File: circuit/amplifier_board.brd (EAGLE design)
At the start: 60 x 30 mm, 17 parts

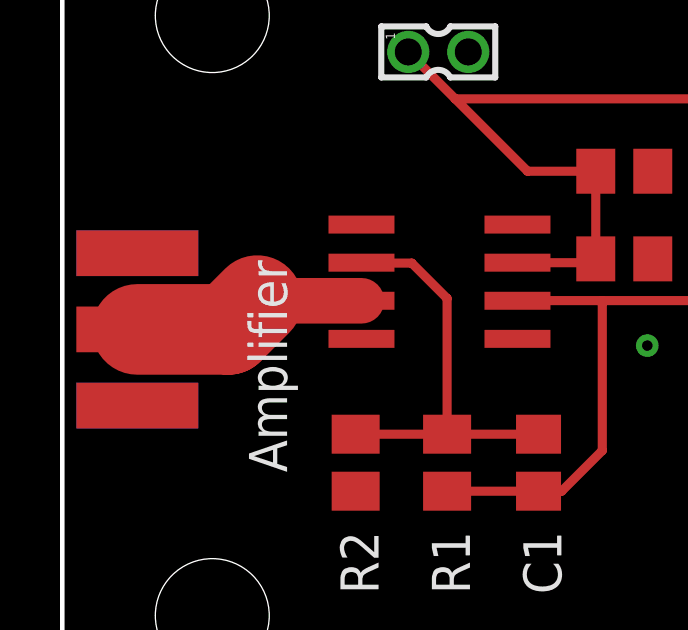
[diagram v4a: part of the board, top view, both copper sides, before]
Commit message: boards: Changes to amplifier board board.
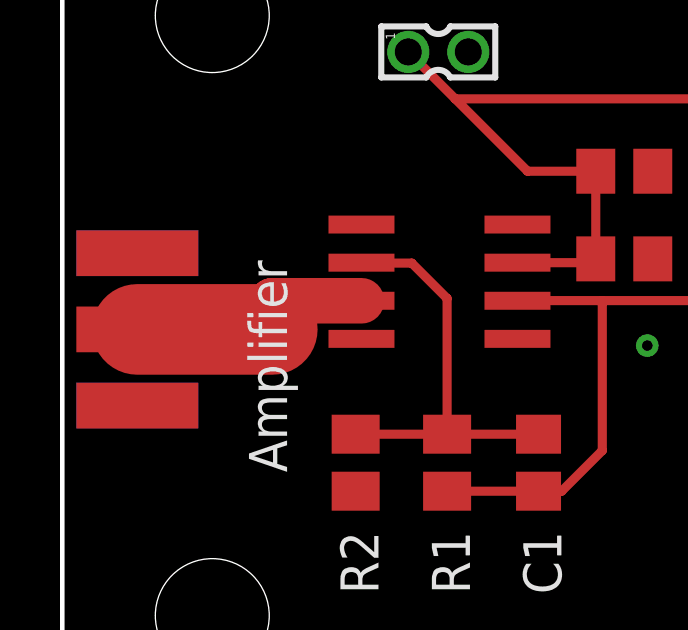
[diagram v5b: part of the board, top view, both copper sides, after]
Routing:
- net IN: track 7.87 -> 8.43 mm
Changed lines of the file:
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@@
 <drawing>
 <settings>
-<setting alwaysvectorfont="no"/>
+<setting alwaysvectorfont="yes"/>
 <setting verticaltext="up"/>
 </settings>
@@
 <contactref element="MAX4104_1" pad="3"/>
 <contactref element="IN" pad="SIG"/>
-<wire x1="2.5" y1="14.54" x2="5.54" y2="14.54" width="3.021" layer="1"/>
-<wire x1="6.5" y1="15.5" x2="5.54" y2="14.54" width="3.021" layer="1"/>
-<wire x1="9.973" y1="15.494" x2="6.506" y2="15.494" width="1.52" layer="1"/>
-<wire x1="6.506" y1="15.494" x2="6.5" y2="15.5" width="1.52" layer="1"/>
+<wire x1="2.5" y1="14.54" x2="7" y2="14.54" width="3.021" layer="1"/>
+<wire x1="9.973" y1="15.494" x2="7" y2="15.494" width="1.52" layer="1"/>
+<wire x1="7" y1="15.494" x2="7" y2="14.54" width="1.52" layer="1"/>
 </signal>
 </signals>

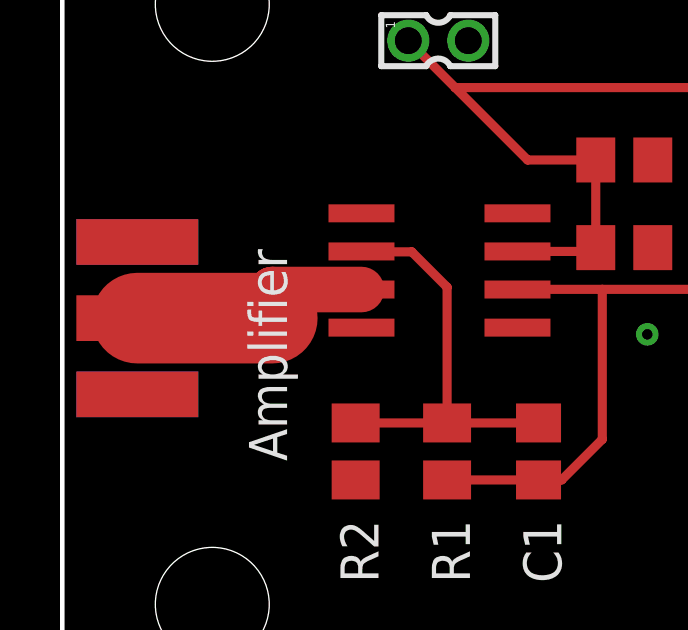
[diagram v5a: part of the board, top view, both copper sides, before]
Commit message: boards: Simplified both boards
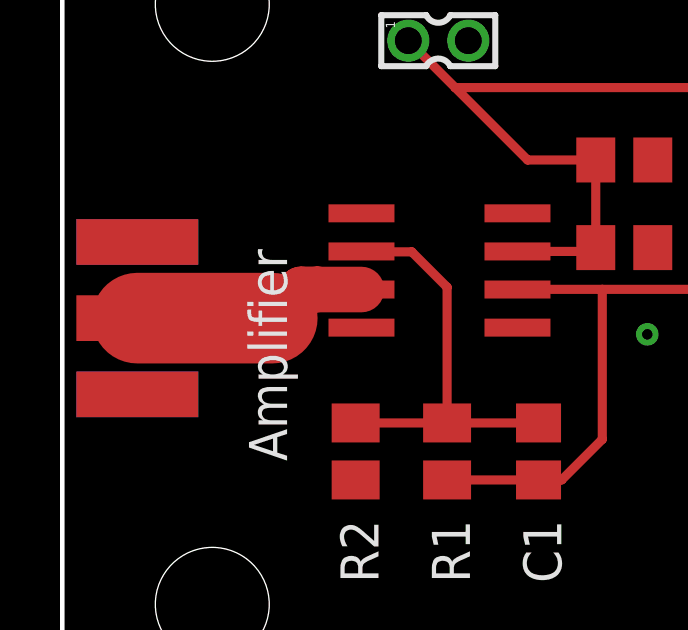
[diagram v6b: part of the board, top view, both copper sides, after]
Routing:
- net IN: track 8.43 -> 7.87 mm
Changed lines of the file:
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@@
 <drawing>
 <settings>
-<setting alwaysvectorfont="yes"/>
+<setting alwaysvectorfont="no"/>
 <setting verticaltext="up"/>
 </settings>
@@
 <contactref element="MAX4104_1" pad="3"/>
 <contactref element="IN" pad="SIG"/>
-<wire x1="2.5" y1="14.54" x2="7" y2="14.54" width="3.021" layer="1"/>
-<wire x1="9.973" y1="15.494" x2="7" y2="15.494" width="1.52" layer="1"/>
-<wire x1="7" y1="15.494" x2="7" y2="14.54" width="1.52" layer="1"/>
+<wire x1="7" y1="14.54" x2="2.5" y2="14.54" width="3.021" layer="1"/>
+<wire x1="9.973" y1="15.494" x2="8.506" y2="15.494" width="1.52" layer="1"/>
+<wire x1="8.506" y1="15.494" x2="8.5" y2="15.5" width="1.52" layer="1"/>
+<wire x1="8.5" y1="15.5" x2="7.96" y2="15.5" width="1.52" layer="1"/>
+<wire x1="7.96" y1="15.5" x2="7" y2="14.54" width="1.52" layer="1"/>
 </signal>
 </signals>

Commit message: boards: Rev00_ss ready
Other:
- board text added: "Gnd"
- board text added: "Out"
- board text added: "Rev00, amplifier board Asher Merrill & Maurik Holtrop, UNH 2018"
- board text added: "Vbias"
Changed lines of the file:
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@@
 <drawing>
 <settings>
-<setting alwaysvectorfont="no"/>
+<setting alwaysvectorfont="yes"/>
 <setting verticaltext="up"/>
 </settings>
@@
 <wire x1="60" y1="0" x2="60" y2="30" width="0.1524" layer="20"/>
 <wire x1="60" y1="30" x2="0" y2="30" width="0.1524" layer="20"/>
+<text x="12" y="22.5" size="1.778" layer="21" rot="R180">Vbias</text>
+<text x="13" y="25" size="1.778" layer="21">Gnd</text>
+<text x="54" y="15" size="1.778" layer="21" rot="R180">Out</text>
+<text x="54" y="17" size="1.778" layer="21" rot="R180">Gnd</text>
+<text x="9" y="2" size="1.2" layer="21">Rev00, amplifier board
+Asher Merrill &amp; Maurik Holtrop, UNH 2018</text>
 </plain>
 <attributes>
@@
 </drawing>
 <compatibility>
+<note version="6.3" minversion="6.2.2" severity="warning">
+Since Version 6.2.2 text objects can contain more than one line,
+which will not be processed correctly with this version.
+</note>
 <note version="8.2" severity="warning">
 Since Version 8.2, EAGLE supports online libraries. The ids

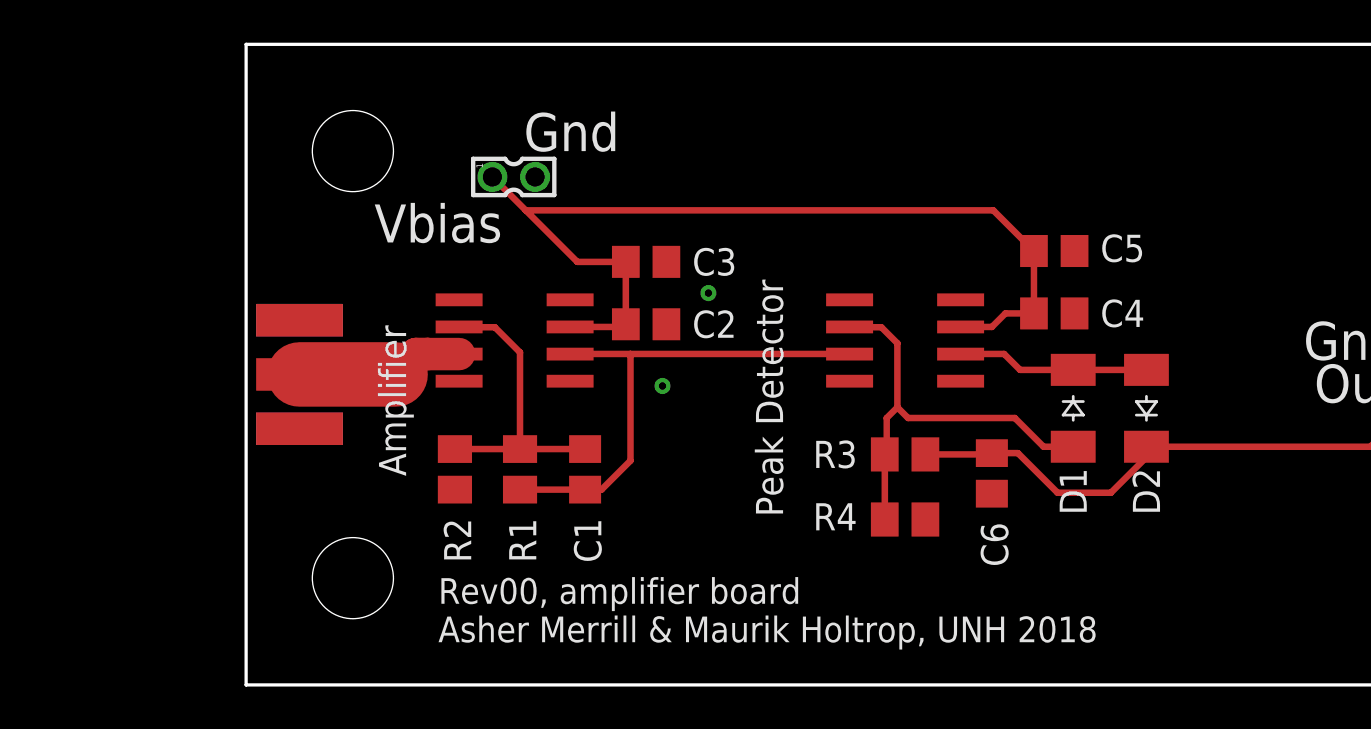
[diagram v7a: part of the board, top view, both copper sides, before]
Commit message: Modified board. Tried to add Spice model.
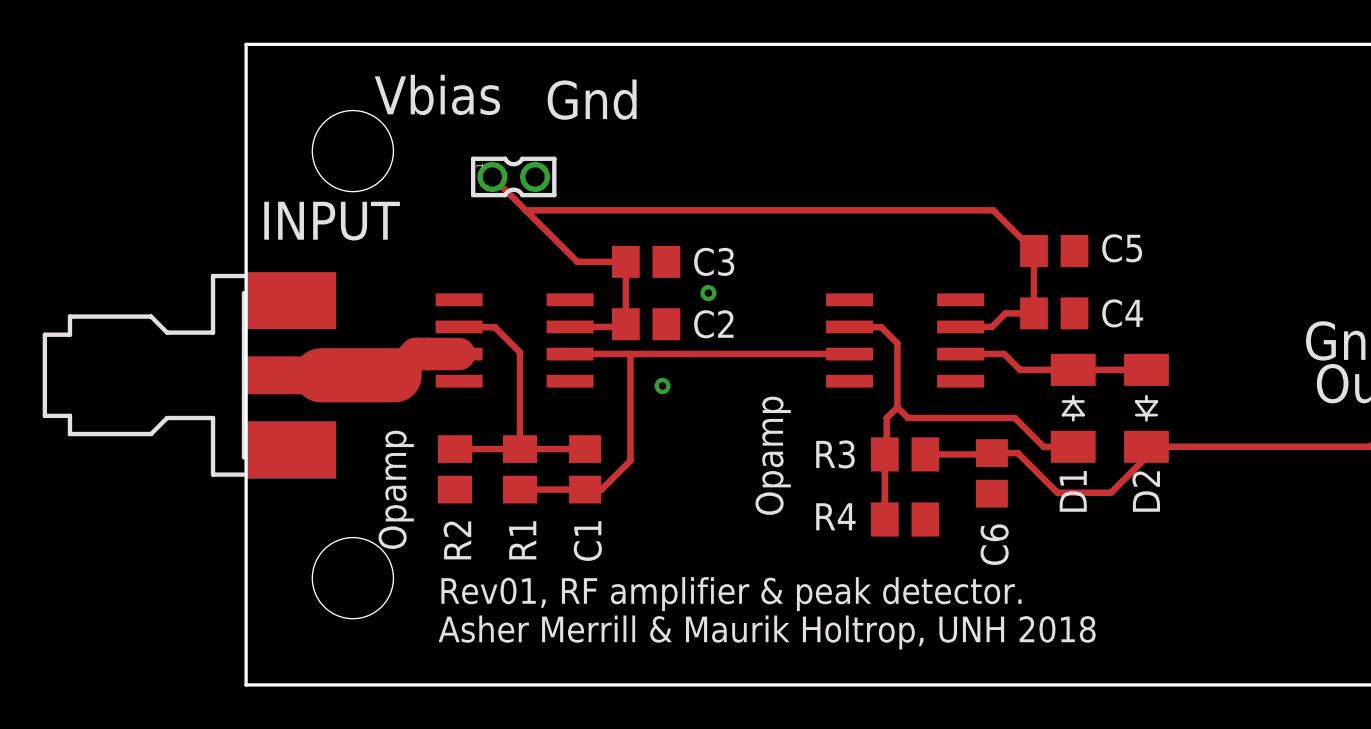
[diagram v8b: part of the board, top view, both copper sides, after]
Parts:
- removed IN: SMA_EDGE, SparkFun-Retired:SMA-EDGE
- added INPUT: SMA-EDGE, 000phys605parts:SMA-EDGE
- MAX4104_1: value Amplifier -> Opamp
- MAX4104_2: value Peak Detector -> Opamp
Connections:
- net GND: now also INPUT.G@1, INPUT.G@2, INPUT.G@3, INPUT.G@4; no longer IN.GND@0, IN.GND@1, IN.GND@2, IN.GND@3
- net IN: now also INPUT.G@0; no longer IN.SIG
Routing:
- net IN: track 7.87 -> 6.89 mm
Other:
- board text added: "Rev01, RF amplifier & peak detector. Asher Merrill & Maurik Holtrop, UNH 2018"
- board text removed: "Rev00, amplifier board Asher Merrill & Maurik Holtrop, UNH 2018"
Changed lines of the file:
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@@
 <drawing>
 <settings>
-<setting alwaysvectorfont="yes"/>
+<setting alwaysvectorfont="no"/>
 <setting verticaltext="up"/>
 </settings>
@@
 <wire x1="60" y1="0" x2="60" y2="30" width="0.1524" layer="20"/>
 <wire x1="60" y1="30" x2="0" y2="30" width="0.1524" layer="20"/>
-<text x="12" y="22.5" size="1.778" layer="21" rot="R180">Vbias</text>
-<text x="13" y="25" size="1.778" layer="21">Gnd</text>
+<text x="12" y="28.5" size="1.778" layer="21" rot="R180">Vbias</text>
+<text x="14" y="26.5" size="1.778" layer="21">Gnd</text>
 <text x="54" y="15" size="1.778" layer="21" rot="R180">Out</text>
 <text x="54" y="17" size="1.778" layer="21" rot="R180">Gnd</text>
-<text x="9" y="2" size="1.2" layer="21">Rev00, amplifier board
+<text x="9" y="2" size="1.2" layer="21">Rev01, RF amplifier &amp; peak detector.
 Asher Merrill &amp; Maurik Holtrop, UNH 2018</text>
 </plain>
@@
 <attribute name="SPICEPREFIX" value="C" x="15.875" y="10.0965" size="1.778" layer="27" rot="R90" display="off"/>
 </element>
-<element name="MAX4104_1" library="000phys605parts" package="SO8" value="Amplifier" x="12.573" y="16.129" smashed="yes" rot="R270">
-<attribute name="VALUE" x="7.493" y="9.779" size="1.27" layer="21" rot="R90"/>
+<element name="MAX4104_1" library="000phys605parts" package="SO8" value="Opamp" x="12.573" y="16.129" smashed="yes" rot="R270">
+<attribute name="SPICEMODEL" value="MAX4104" x="12.573" y="16.129" size="1.778" layer="27" rot="R270" display="off"/>
+<attribute name="SPICEPREFIX" value="X" x="12.573" y="16.129" size="1.778" layer="27" rot="R270" display="off"/>
+<attribute name="VALUE" x="7.493" y="6.279" size="1.27" layer="21" rot="R90"/>
 </element>
 <element name="R1" library="rcl" library_urn="urn:adsk.eagle:library:334" package="M0805" package3d_urn="urn:adsk.eagle:package:23556/1" value="10k" x="12.827" y="10.0965" smashed="yes" rot="R270">
@@
 <attribute name="SPICEPREFIX" value="C" x="18.7325" y="16.891" size="1.778" layer="27" display="off"/>
 </element>
-<element name="SUP" library="con-garry" library_urn="urn:adsk.eagle:library:147" package="332-02" package3d_urn="urn:adsk.eagle:package:6810/1" value="332-02" x="12.533" y="23.789" smashed="yes" rot="R270"/>
-<element name="MAX4104_2" library="000phys605parts" package="SO8" value="Peak Detector" x="30.861" y="16.129" smashed="yes" rot="R270">
+<element name="SUP" library="con-garry" library_urn="urn:adsk.eagle:library:147" package="332-02" package3d_urn="urn:adsk.eagle:package:6810/1" value="332-02" x="12.533" y="23.789" smashed="yes" rot="R270">
+<attribute name="SPICEMODEL" value="VoltageSource" x="12.533" y="23.789" size="1.778" layer="27" rot="R270" display="off"/>
+<attribute name="SPICEPREFIX" value="X" x="12.533" y="23.789" size="1.778" layer="27" rot="R270" display="off"/>
+</element>
+<element name="MAX4104_2" library="000phys605parts" package="SO8" value="Opamp" x="30.861" y="16.129" smashed="yes" rot="R270">
+<attribute name="SPICEMODEL" value="MAX4104" x="30.861" y="16.129" size="1.778" layer="27" rot="R270" display="off"/>
+<attribute name="SPICEPREFIX" value="X" x="30.861" y="16.129" size="1.778" layer="27" rot="R270" display="off"/>
 <attribute name="VALUE" x="25.146" y="7.874" size="1.27" layer="21" rot="R90"/>
 </element>
@@
 <attribute name="SPICEPREFIX" value="C" x="34.925" y="9.906" size="1.778" layer="27" rot="R270" display="off"/>
 </element>
-<element name="IN" library="SparkFun-Retired" package="SMA-EDGE" value="SMA_EDGE" x="2.5" y="12" rot="R90"/>
 <element name="D1" library="diode" library_urn="urn:adsk.eagle:library:210" package="SOD-123_MINI-SMA" package3d_urn="urn:adsk.eagle:package:43457/2" value="MBR0540CT-ND" x="38.735" y="12.954" smashed="yes" rot="R270">
 <attribute name="NAME" x="38.1" y="10.16" size="1.27" layer="25" rot="R270"/>
+<attribute name="SPICEMODEL" value="DMBR0540" x="38.735" y="12.954" size="1.778" layer="27" rot="R270" display="off"/>
+<attribute name="SPICEPREFIX" value="D" x="38.735" y="12.954" size="1.778" layer="27" rot="R270" display="off"/>
 </element>
 <element name="D2" library="diode" library_urn="urn:adsk.eagle:library:210" package="SOD-123_MINI-SMA" package3d_urn="urn:adsk.eagle:package:43457/2" value="MBR0540CT-ND" x="42.164" y="12.954" smashed="yes" rot="R90">
 <attribute name="NAME" x="41.529" y="10.16" size="1.27" layer="25" rot="R270"/>
-</element>
-<element name="SUP1" library="con-garry" library_urn="urn:adsk.eagle:library:147" package="332-02" package3d_urn="urn:adsk.eagle:package:6810/1" value="332-02" x="55.5" y="15" smashed="yes"/>
+<attribute name="SPICEMODEL" value="DMBR0540" x="42.164" y="12.954" size="1.778" layer="27" rot="R90" display="off"/>
+<attribute name="SPICEPREFIX" value="D" x="42.164" y="12.954" size="1.778" layer="27" rot="R90" display="off"/>
+</element>
+<element name="SUP1" library="con-garry" library_urn="urn:adsk.eagle:library:147" package="332-02" package3d_urn="urn:adsk.eagle:package:6810/1" value="332-02" x="55.5" y="15" smashed="yes">
+<attribute name="SPICEMODEL" value="TerminalOut" x="55.5" y="15" size="1.778" layer="27" display="off"/>
+<attribute name="SPICEPREFIX" value="X" x="55.5" y="15" size="1.778" layer="27" display="off"/>
+</element>
+<element name="INPUT" library="000phys605parts" package="SMA-EDGE" value="SMA-EDGE" x="0" y="14.5">
+<attribute name="SPICEPREFIX" value="V" x="0" y="14.5" size="1.778" layer="27" display="off"/>
+</element>
 </elements>
 <signals>
@@
 <contactref element="MAX4104_2" pad="4"/>
 <contactref element="C6" pad="2"/>
-<contactref element="IN" pad="GND@3"/>
-<contactref element="IN" pad="GND@2"/>
-<contactref element="IN" pad="GND@1"/>
-<contactref element="IN" pad="GND@0"/>
 <polygon width="0.184" layer="1">
 <vertex x="0" y="30"/>
@@
 <via x="19.5" y="14" extent="1-16" drill="0.35"/>
 <via x="21.65" y="18.35" extent="1-16" drill="0.35"/>
+<contactref element="INPUT" pad="G@3"/>
+<contactref element="INPUT" pad="G@2"/>
+<contactref element="INPUT" pad="G@1"/>
+<contactref element="INPUT" pad="G@4"/>
+<wire x1="38.796" y1="17.399" x2="55.5" y2="16" width="0" layer="19" extent="1-1"/>
+<wire x1="38.796" y1="20.32" x2="38.796" y2="17.399" width="0" layer="19" extent="1-1"/>
+<wire x1="34.925" y1="8.956" x2="38.796" y2="17.399" width="0" layer="19" extent="1-1"/>
+<wire x1="31.811" y1="7.747" x2="34.925" y2="8.956" width="0" layer="19" extent="1-1"/>
+<wire x1="28.261" y1="14.224" x2="31.811" y2="7.747" width="0" layer="19" extent="1-1"/>
+<wire x1="21.65" y1="18.35" x2="28.261" y2="14.224" width="0" layer="19" extent="1-1"/>
+<wire x1="19.6825" y1="19.812" x2="21.65" y2="18.35" width="0" layer="19" extent="1-1"/>
+<wire x1="19.6825" y1="16.891" x2="21.65" y2="18.35" width="0" layer="19" extent="1-1"/>
+<wire x1="19.5" y1="14" x2="19.6825" y2="16.891" width="0" layer="19" extent="1-1"/>
+<wire x1="13.533" y1="23.789" x2="19.6825" y2="19.812" width="0" layer="19" extent="1-1"/>
+<wire x1="9.973" y1="14.224" x2="19.5" y2="14" width="0" layer="19" extent="1-1"/>
+<wire x1="9.779" y1="9.1465" x2="9.973" y2="14.224" width="0" layer="19" extent="1-1"/>
+<wire x1="2.1154" y1="17.9946" x2="9.779" y2="9.1465" width="0" layer="19" extent="1-16"/>
+<wire x1="2.1154" y1="17.9946" x2="2.1154" y2="17.9946" width="0" layer="19" extent="1-16"/>
+<wire x1="2.1154" y1="11.0054" x2="2.1154" y2="17.9946" width="0" layer="19" extent="1-16"/>
+<wire x1="2.1154" y1="11.0054" x2="2.1154" y2="11.0054" width="0" layer="19" extent="1-16"/>
 </signal>
 <signal name="AMP">
@@
 <signal name="IN" class="1">
 <contactref element="MAX4104_1" pad="3"/>
-<contactref element="IN" pad="SIG"/>
-<wire x1="7" y1="14.54" x2="2.5" y2="14.54" width="3.021" layer="1"/>
 <wire x1="9.973" y1="15.494" x2="8.506" y2="15.494" width="1.52" layer="1"/>
 <wire x1="8.506" y1="15.494" x2="8.5" y2="15.5" width="1.52" layer="1"/>
 <wire x1="8.5" y1="15.5" x2="7.96" y2="15.5" width="1.52" layer="1"/>
 <wire x1="7.96" y1="15.5" x2="7" y2="14.54" width="1.52" layer="1"/>
+<contactref element="INPUT" pad="G@0"/>
+<wire x1="7" y1="14.54" x2="6.96" y2="14.5" width="0.1524" layer="1"/>
+<wire x1="6.96" y1="14.5" x2="3.5" y2="14.5" width="2.54" layer="1"/>
+<wire x1="2.1154" y1="14.5" x2="3.5" y2="14.5" width="0" layer="19" extent="1-1"/>
 </signal>
 </signals>
